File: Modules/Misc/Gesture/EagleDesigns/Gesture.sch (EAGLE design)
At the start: 26 parts, among them Q1 16MHz, U1 NRF24L01ALT1, U2 ATMEGA328P_TQFP, U3 LSM9DS1, Y1 ANTENNA2SMD5

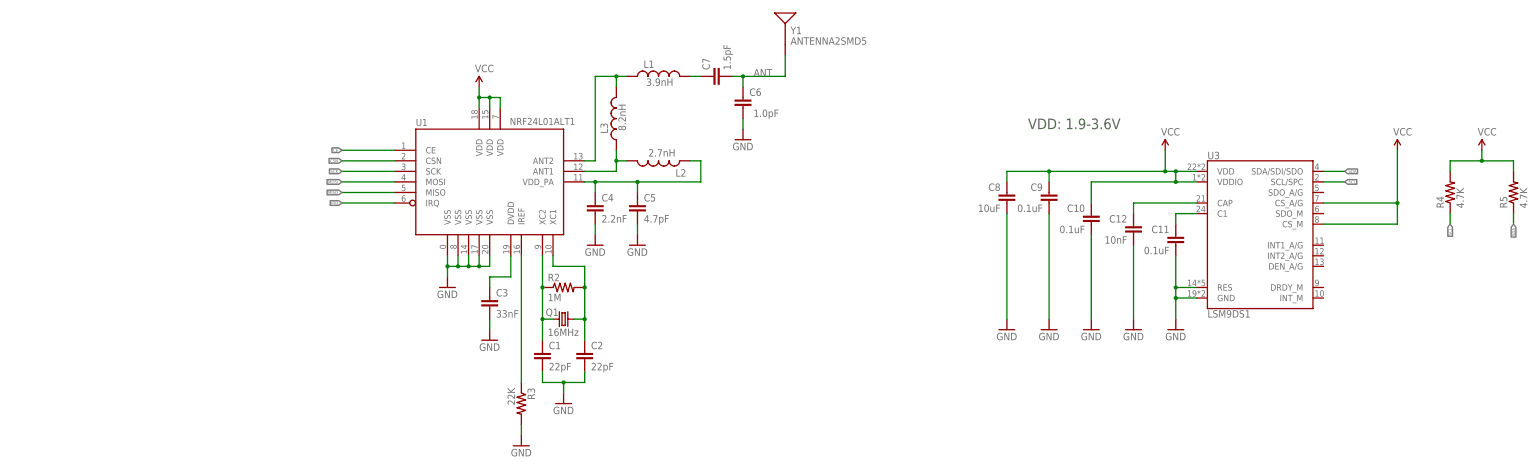
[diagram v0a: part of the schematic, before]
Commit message: updated the PCB/Schematics for the Gesture module
TODO: now I only need to build the middle PCB (ATmega328p + IMU)
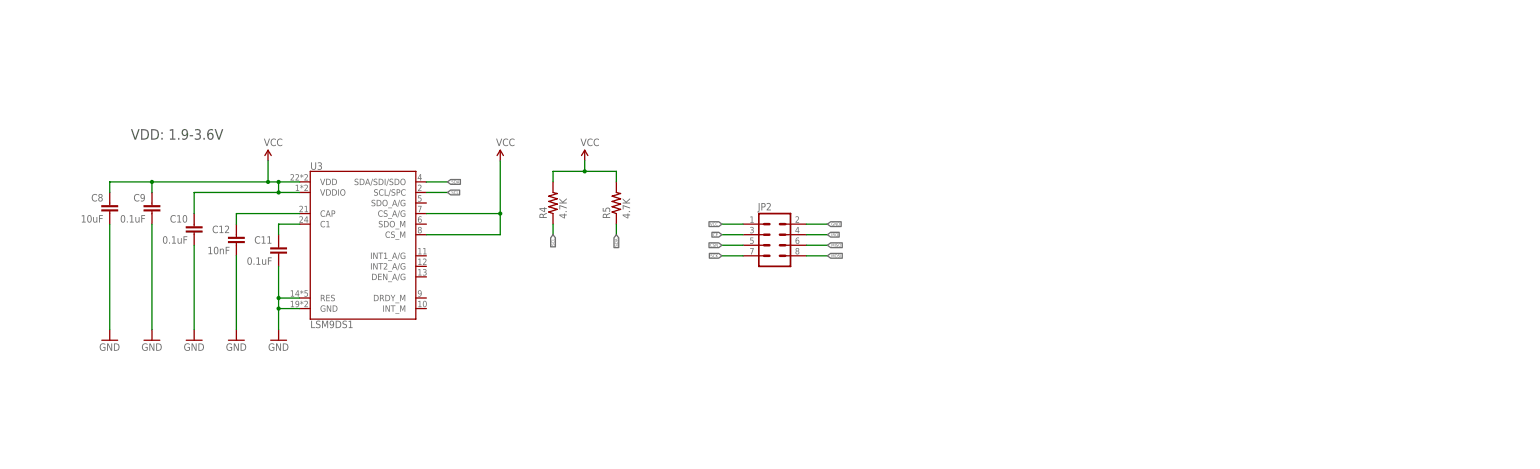
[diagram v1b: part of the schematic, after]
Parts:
- removed C1, C2: 22pF, SparkFun:CAP0402-CAP
- removed C3: 33nF, SparkFun:CAP0402-CAP
- removed C4: 2.2nF, SparkFun:CAP0402-CAP
- removed C5: 4.7pF, SparkFun:CAP0402-CAP
- removed C6: 1.0pF, SparkFun:CAP0402-CAP
- removed C7: 1.5pF, SparkFun:CAP0402-CAP
- removed L1: 3.9nH, SparkFun:INDUCTOR0402
- removed L2: 2.7nH, SparkFun:INDUCTOR0402
- removed L3: 8.2nH, SparkFun:INDUCTOR0402
- removed Q1: 16MHz, SparkFun:CRYSTAL5X3
- removed R2: 1M, SparkFun:RESISTOR0402-RES
- removed R3: 22K, SparkFun:RESISTOR0402-RES
- removed U1: NRF24L01ALT1, Testing:NRF24L01ALT1
- removed Y1: ANTENNA2SMD5, SparkFun:ANTENNA2SMD5
- added JP2: (no value), MakerWear:M04X2_0.05"
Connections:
- removed net ANT: C6.2, C7.2, Y1.SIGNAL
- removed net N$1: C1.1, Q1.1, R2.1, U1.XC2
- removed net N$2: C2.1, Q1.2, R2.2, U1.XC1
- removed net N$3: L2.2, L3.1, U1.ANT1
- removed net N$4: R3.1, U1.IREF
- removed net N$5: C3.1, U1.DVDD
- removed net N$6: L1.1, L3.2, U1.ANT2
- removed net N$7: C4.1, C5.1, L2.1, U1.VDD_PA
- removed net N$9: C7.1, L1.2
- net CE: now also JP2.3; no longer U1.CE
- net CSN: now also JP2.5; no longer U1.CSN
- net GND: now also JP2.2; no longer C1.2, C2.2, C3.2, C4.2, C5.2, C6.1, R3.2, U1.VSS@0, U1.VSS@14, U1.VSS@17, U1.VSS@20, U1.VSS@8
- net IRQ: now also JP2.4; no longer U1.IRQ
- net MISO: now also JP2.6; no longer U1.MISO
- net MOSI: now also JP2.8; no longer U1.MOSI
- net SCK: now also JP2.7; no longer U1.SCK
- net VCC: now also JP2.1; no longer U1.VDD@15, U1.VDD@18, U1.VDD@7
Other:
- moved on the sheet: C10, C11, C12, C8, C9, R4, R5, U3

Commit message: finished the Gesture module
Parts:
- added JP3: (no value), SparkFun-Connectors:M02LOCK
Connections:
- net RX: now also JP3.1
- net TX: now also JP3.2
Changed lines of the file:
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@@
 <grid distance="0.1" unitdist="inch" unit="inch" style="lines" multiple="1" display="no" altdistance="0.01" altunitdist="inch" altunit="inch"/>
 <layers>
-<layer number="1" name="Top" color="4" fill="1" visible="no" active="no"/>
-<layer number="2" name="Route2" color="1" fill="3" visible="no" active="no"/>
-<layer number="15" name="Route15" color="4" fill="6" visible="no" active="no"/>
-<layer number="16" name="Bottom" color="1" fill="1" visible="no" active="no"/>
-<layer number="17" name="Pads" color="2" fill="1" visible="no" active="no"/>
-<layer number="18" name="Vias" color="2" fill="1" visible="no" active="no"/>
-<layer number="19" name="Unrouted" color="6" fill="1" visible="no" active="no"/>
-<layer number="20" name="Dimension" color="15" fill="1" visible="no" active="no"/>
-<layer number="21" name="tPlace" color="16" fill="1" visible="no" active="no"/>
-<layer number="22" name="bPlace" color="7" fill="1" visible="no" active="no"/>
-<layer number="23" name="tOrigins" color="15" fill="1" visible="no" active="no"/>
-<layer number="24" name="bOrigins" color="15" fill="1" visible="no" active="no"/>
-<layer number="25" name="tNames" color="7" fill="1" visible="no" active="no"/>
-<layer number="26" name="bNames" color="7" fill="1" visible="no" active="no"/>
-<layer number="27" name="tValues" color="7" fill="1" visible="no" active="no"/>
-<layer number="28" name="bValues" color="7" fill="1" visible="no" active="no"/>
+<layer number="1" name="Top" color="4" fill="1" visible="yes" active="no"/>
+<layer number="2" name="Route2" color="1" fill="3" visible="yes" active="no"/>
+<layer number="15" name="Route15" color="4" fill="6" visible="yes" active="no"/>
+<layer number="16" name="Bottom" color="1" fill="1" visible="yes" active="no"/>
+<layer number="17" name="Pads" color="2" fill="1" visible="yes" active="no"/>
+<layer number="18" name="Vias" color="2" fill="1" visible="yes" active="no"/>
+<layer number="19" name="Unrouted" color="6" fill="1" visible="yes" active="no"/>
+<layer number="20" name="Dimension" color="15" fill="1" visible="yes" active="no"/>
+<layer number="21" name="tPlace" color="7" fill="1" visible="yes" active="no"/>
+<layer number="22" name="bPlace" color="7" fill="1" visible="yes" active="no"/>
+<layer number="23" name="tOrigins" color="15" fill="1" visible="yes" active="no"/>
+<layer number="24" name="bOrigins" color="15" fill="1" visible="yes" active="no"/>
+<layer number="25" name="tNames" color="7" fill="1" visible="yes" active="no"/>
+<layer number="26" name="bNames" color="7" fill="1" visible="yes" active="no"/>
+<layer number="27" name="tValues" color="7" fill="1" visible="yes" active="no"/>
+<layer number="28" name="bValues" color="7" fill="1" visible="yes" active="no"/>
 <layer number="29" name="tStop" color="7" fill="3" visible="no" active="no"/>
 <layer number="30" name="bStop" color="7" fill="6" visible="no" active="no"/>
@@
 <layer number="35" name="tGlue" color="7" fill="4" visible="no" active="no"/>
 <layer number="36" name="bGlue" color="7" fill="5" visible="no" active="no"/>
-<layer number="37" name="tTest" color="7" fill="1" visible="no" active="no"/>
-<layer number="38" name="bTest" color="7" fill="1" visible="no" active="no"/>
+<layer number="37" name="tTest" color="7" fill="1" visible="yes" active="no"/>
+<layer number="38" name="bTest" color="7" fill="1" visible="yes" active="no"/>
 <layer number="39" name="tKeepout" color="4" fill="11" visible="no" active="no"/>
 <layer number="40" name="bKeepout" color="1" fill="11" visible="no" active="no"/>
@@
 <layer number="44" name="Drills" color="7" fill="1" visible="no" active="no"/>
 <layer number="45" name="Holes" color="7" fill="1" visible="no" active="no"/>
-<layer number="46" name="Milling" color="3" fill="1" visible="no" active="no"/>
-<layer number="47" name="Measures" color="7" fill="1" visible="no" active="no"/>
-<layer number="48" name="Document" color="7" fill="1" visible="no" active="no"/>
-<layer number="49" name="Reference" color="7" fill="1" visible="no" active="no"/>
-<layer number="50" name="dxf" color="7" fill="1" visible="no" active="no"/>
-<layer number="51" name="tDocu" color="14" fill="1" visible="no" active="no"/>
-<layer number="52" name="bDocu" color="7" fill="1" visible="no" active="no"/>
-<layer number="53" name="tGND_GNDA" color="7" fill="9" visible="no" active="no"/>
-<layer number="54" name="bGND_GNDA" color="1" fill="9" visible="no" active="no"/>
-<layer number="56" name="wert" color="7" fill="1" visible="no" active="no"/>
-<layer number="57" name="tCAD" color="7" fill="1" visible="no" active="no"/>
-<layer number="59" name="tCarbon" color="7" fill="1" visible="no" active="no"/>
-<layer number="60" name="bCarbon" color="7" fill="1" visible="no" active="no"/>
+<layer number="46" name="Milling" color="3" fill="1" visible="yes" active="no"/>
+<layer number="47" name="Measures" color="7" fill="1" visible="yes" active="no"/>
+<layer number="48" name="Document" color="7" fill="1" visible="yes" active="no"/>
+<layer number="49" name="Reference" color="7" fill="1" visible="yes" active="no"/>
+<layer number="50" name="dxf" color="7" fill="1" visible="yes" active="no"/>
+<layer number="51" name="tDocu" color="7" fill="1" visible="yes" active="no"/>
+<layer number="52" name="bDocu" color="7" fill="1" visible="yes" active="no"/>
+<layer number="53" name="tGND_GNDA" color="7" fill="9" visible="yes" active="no"/>
+<layer number="54" name="bGND_GNDA" color="1" fill="9" visible="yes" active="no"/>
+<layer number="56" name="wert" color="7" fill="1" visible="yes" active="no"/>
+<layer number="57" name="tCAD" color="7" fill="1" visible="yes" active="no"/>
+<layer number="59" name="tCarbon" color="7" fill="1" visible="yes" active="no"/>
+<layer number="60" name="bCarbon" color="7" fill="1" visible="yes" active="no"/>
 <layer number="90" name="Modules" color="5" fill="1" visible="yes" active="yes"/>
 <layer number="91" name="Nets" color="2" fill="1" visible="yes" active="yes"/>
@@
 <part name="P+4" library="SparkFun" deviceset="VCC" device=""/>
 <part name="JP2" library="MakerWear" deviceset="M04X2_0.05&quot;" device=""/>
+<part name="JP3" library="SparkFun-Connectors" deviceset="M02" device="LOCK"/>
 </parts>
 <sheets>
@@
 <instance part="P+4" gate="1" x="353.06" y="30.48"/>
 <instance part="JP2" gate="G$1" x="398.78" y="10.16"/>
+<instance part="JP3" gate="G$1" x="398.78" y="-5.08" rot="R180"/>
 </instances>
 <busses>
@@
 <label x="198.12" y="20.32" size="0.762" layer="95" xref="yes"/>
 </segment>
+<segment>
+<pinref part="JP3" gate="G$1" pin="1"/>
+<wire x1="391.16" y1="-5.08" x2="386.08" y2="-5.08" width="0.1524" layer="91"/>
+<label x="386.08" y="-5.08" size="0.762" layer="95" rot="R180" xref="yes"/>
+</segment>
 </net>
 <net name="TX" class="0">
@@
 <label x="198.12" y="17.78" size="0.762" layer="95" xref="yes"/>
 </segment>
-</net>
+<segment>
+<pinref part="JP3" gate="G$1" pin="2"/>
+<wire x1="391.16" y1="-7.62" x2="386.08" y2="-7.62" width="0.1524" layer="91"/>
+<label x="386.08" y="-7.62" size="0.762" layer="95" rot="R180" xref="yes"/>
+</segment>
+</net>

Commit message: another round of minor fixes
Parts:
- JP3: device SparkFun-Connectors:M02LOCK -> SparkFun-Connectors:M03PTH
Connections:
- net RESET: now also JP3.3
- net RX: now also JP3.2; no longer JP3.1
- net TX: now also JP3.1; no longer JP3.2
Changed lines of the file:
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@@
 <grid distance="0.1" unitdist="inch" unit="inch" style="lines" multiple="1" display="no" altdistance="0.01" altunitdist="inch" altunit="inch"/>
 <layers>
-<layer number="1" name="Top" color="4" fill="1" visible="yes" active="no"/>
-<layer number="2" name="Route2" color="1" fill="3" visible="yes" active="no"/>
-<layer number="15" name="Route15" color="4" fill="6" visible="yes" active="no"/>
-<layer number="16" name="Bottom" color="1" fill="1" visible="yes" active="no"/>
-<layer number="17" name="Pads" color="2" fill="1" visible="yes" active="no"/>
-<layer number="18" name="Vias" color="2" fill="1" visible="yes" active="no"/>
-<layer number="19" name="Unrouted" color="6" fill="1" visible="yes" active="no"/>
-<layer number="20" name="Dimension" color="15" fill="1" visible="yes" active="no"/>
-<layer number="21" name="tPlace" color="7" fill="1" visible="yes" active="no"/>
-<layer number="22" name="bPlace" color="7" fill="1" visible="yes" active="no"/>
-<layer number="23" name="tOrigins" color="15" fill="1" visible="yes" active="no"/>
-<layer number="24" name="bOrigins" color="15" fill="1" visible="yes" active="no"/>
-<layer number="25" name="tNames" color="7" fill="1" visible="yes" active="no"/>
-<layer number="26" name="bNames" color="7" fill="1" visible="yes" active="no"/>
-<layer number="27" name="tValues" color="7" fill="1" visible="yes" active="no"/>
-<layer number="28" name="bValues" color="7" fill="1" visible="yes" active="no"/>
+<layer number="1" name="Top" color="4" fill="1" visible="no" active="no"/>
+<layer number="2" name="Route2" color="1" fill="3" visible="no" active="no"/>
+<layer number="15" name="Route15" color="4" fill="6" visible="no" active="no"/>
+<layer number="16" name="Bottom" color="1" fill="1" visible="no" active="no"/>
+<layer number="17" name="Pads" color="2" fill="1" visible="no" active="no"/>
+<layer number="18" name="Vias" color="2" fill="1" visible="no" active="no"/>
+<layer number="19" name="Unrouted" color="6" fill="1" visible="no" active="no"/>
+<layer number="20" name="Dimension" color="15" fill="1" visible="no" active="no"/>
+<layer number="21" name="tPlace" color="7" fill="1" visible="no" active="no"/>
+<layer number="22" name="bPlace" color="7" fill="1" visible="no" active="no"/>
+<layer number="23" name="tOrigins" color="15" fill="1" visible="no" active="no"/>
+<layer number="24" name="bOrigins" color="15" fill="1" visible="no" active="no"/>
+<layer number="25" name="tNames" color="7" fill="1" visible="no" active="no"/>
+<layer number="26" name="bNames" color="7" fill="1" visible="no" active="no"/>
+<layer number="27" name="tValues" color="7" fill="1" visible="no" active="no"/>
+<layer number="28" name="bValues" color="7" fill="1" visible="no" active="no"/>
 <layer number="29" name="tStop" color="7" fill="3" visible="no" active="no"/>
 <layer number="30" name="bStop" color="7" fill="6" visible="no" active="no"/>
@@
 <layer number="35" name="tGlue" color="7" fill="4" visible="no" active="no"/>
 <layer number="36" name="bGlue" color="7" fill="5" visible="no" active="no"/>
-<layer number="37" name="tTest" color="7" fill="1" visible="yes" active="no"/>
-<layer number="38" name="bTest" color="7" fill="1" visible="yes" active="no"/>
+<layer number="37" name="tTest" color="7" fill="1" visible="no" active="no"/>
+<layer number="38" name="bTest" color="7" fill="1" visible="no" active="no"/>
 <layer number="39" name="tKeepout" color="4" fill="11" visible="no" active="no"/>
 <layer number="40" name="bKeepout" color="1" fill="11" visible="no" active="no"/>
@@
 <layer number="44" name="Drills" color="7" fill="1" visible="no" active="no"/>
 <layer number="45" name="Holes" color="7" fill="1" visible="no" active="no"/>
-<layer number="46" name="Milling" color="3" fill="1" visible="yes" active="no"/>
-<layer number="47" name="Measures" color="7" fill="1" visible="yes" active="no"/>
-<layer number="48" name="Document" color="7" fill="1" visible="yes" active="no"/>
-<layer number="49" name="Reference" color="7" fill="1" visible="yes" active="no"/>
-<layer number="50" name="dxf" color="7" fill="1" visible="yes" active="no"/>
-<layer number="51" name="tDocu" color="7" fill="1" visible="yes" active="no"/>
-<layer number="52" name="bDocu" color="7" fill="1" visible="yes" active="no"/>
-<layer number="53" name="tGND_GNDA" color="7" fill="9" visible="yes" active="no"/>
-<layer number="54" name="bGND_GNDA" color="1" fill="9" visible="yes" active="no"/>
-<layer number="56" name="wert" color="7" fill="1" visible="yes" active="no"/>
-<layer number="57" name="tCAD" color="7" fill="1" visible="yes" active="no"/>
-<layer number="59" name="tCarbon" color="7" fill="1" visible="yes" active="no"/>
-<layer number="60" name="bCarbon" color="7" fill="1" visible="yes" active="no"/>
+<layer number="46" name="Milling" color="3" fill="1" visible="no" active="no"/>
+<layer number="47" name="Measures" color="7" fill="1" visible="no" active="no"/>
+<layer number="48" name="Document" color="7" fill="1" visible="no" active="no"/>
+<layer number="49" name="Reference" color="7" fill="1" visible="no" active="no"/>
+<layer number="50" name="dxf" color="7" fill="1" visible="no" active="no"/>
+<layer number="51" name="tDocu" color="7" fill="1" visible="no" active="no"/>
+<layer number="52" name="bDocu" color="7" fill="1" visible="no" active="no"/>
+<layer number="53" name="tGND_GNDA" color="7" fill="9" visible="no" active="no"/>
+<layer number="54" name="bGND_GNDA" color="1" fill="9" visible="no" active="no"/>
+<layer number="56" name="wert" color="7" fill="1" visible="no" active="no"/>
+<layer number="57" name="tCAD" color="7" fill="1" visible="no" active="no"/>
+<layer number="59" name="tCarbon" color="7" fill="1" visible="no" active="no"/>
+<layer number="60" name="bCarbon" color="7" fill="1" visible="no" active="no"/>
 <layer number="90" name="Modules" color="5" fill="1" visible="yes" active="yes"/>
 <layer number="91" name="Nets" color="2" fill="1" visible="yes" active="yes"/>
@@
 <part name="P+4" library="SparkFun" deviceset="VCC" device=""/>
 <part name="JP2" library="MakerWear" deviceset="M04X2_0.05&quot;" device=""/>
-<part name="JP3" library="SparkFun-Connectors" deviceset="M02" device="LOCK"/>
+<part name="JP3" library="SparkFun-Connectors" deviceset="M03" device="PTH"/>
 </parts>
 <sheets>
@@
 <instance part="P+4" gate="1" x="353.06" y="30.48"/>
 <instance part="JP2" gate="G$1" x="398.78" y="10.16"/>
-<instance part="JP3" gate="G$1" x="398.78" y="-5.08" rot="R180"/>
+<instance part="JP3" gate="G$1" x="399.288" y="-7.62" rot="R180"/>
 </instances>
 <busses>
@@
 <label x="139.7" y="43.18" size="0.762" layer="95" rot="R180" xref="yes"/>
 </segment>
+<segment>
+<pinref part="JP3" gate="G$1" pin="3"/>
+<wire x1="391.668" y1="-10.16" x2="386.08" y2="-10.16" width="0.1524" layer="91"/>
+<label x="386.08" y="-10.16" size="0.762" layer="95" rot="R180" xref="yes"/>
+</segment>
 </net>
 <net name="RX" class="0">
@@
 </segment>
 <segment>
-<pinref part="JP3" gate="G$1" pin="1"/>
-<wire x1="391.16" y1="-5.08" x2="386.08" y2="-5.08" width="0.1524" layer="91"/>
-<label x="386.08" y="-5.08" size="0.762" layer="95" rot="R180" xref="yes"/>
+<wire x1="391.668" y1="-7.62" x2="386.08" y2="-7.62" width="0.1524" layer="91"/>
+<label x="386.08" y="-7.62" size="0.762" layer="95" rot="R180" xref="yes"/>
+<pinref part="JP3" gate="G$1" pin="2"/>
 </segment>
 </net>
@@
 </segment>
 <segment>
-<pinref part="JP3" gate="G$1" pin="2"/>
-<wire x1="391.16" y1="-7.62" x2="386.08" y2="-7.62" width="0.1524" layer="91"/>
-<label x="386.08" y="-7.62" size="0.762" layer="95" rot="R180" xref="yes"/>
-</segment>
-</net>
+<wire x1="391.668" y1="-5.08" x2="386.08" y2="-5.08" width="0.1524" layer="91"/>
+<label x="386.08" y="-5.08" size="0.762" layer="95" rot="R180" xref="yes"/>
+<pinref part="JP3" gate="G$1" pin="1"/>
+</segment>
+</net>
